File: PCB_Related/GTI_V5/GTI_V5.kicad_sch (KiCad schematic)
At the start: 165 parts, among them IC3 MAX253CSA+, IC4 AMC1306M25QDWVRQ1, IC5 AMC1306M25QDWVRQ1, IC6 AMC1306M25QDWVRQ1, IC7 MAX253CSA+, IC8 MAX253CSA+, IC9 AMC1306M25QDWVRQ1, J1 Screw_Terminal_01x03, J2 Screw_Terminal_01x02, J3 Screw_Terminal_01x02, J4 Conn_01x05_Male, J5 Conn_01x02_Male, J6 Conn_01x02_Male, K1 G5LE-1, K2 G5LE-1, Q1 BUZ11, Q2 2N7002, Q3 BUZ11, Q4 BUZ11, Q5 BUZ11, T1 760390014, T2 760390014, T3 760390014, U1 STM32L475RCTx, U2 UCC21520ADW, U3 AZ1117-5.0, U4 NCP1117-3.3_SOT223, U5 UCC21520ADW, Y1 Crystal_GND24

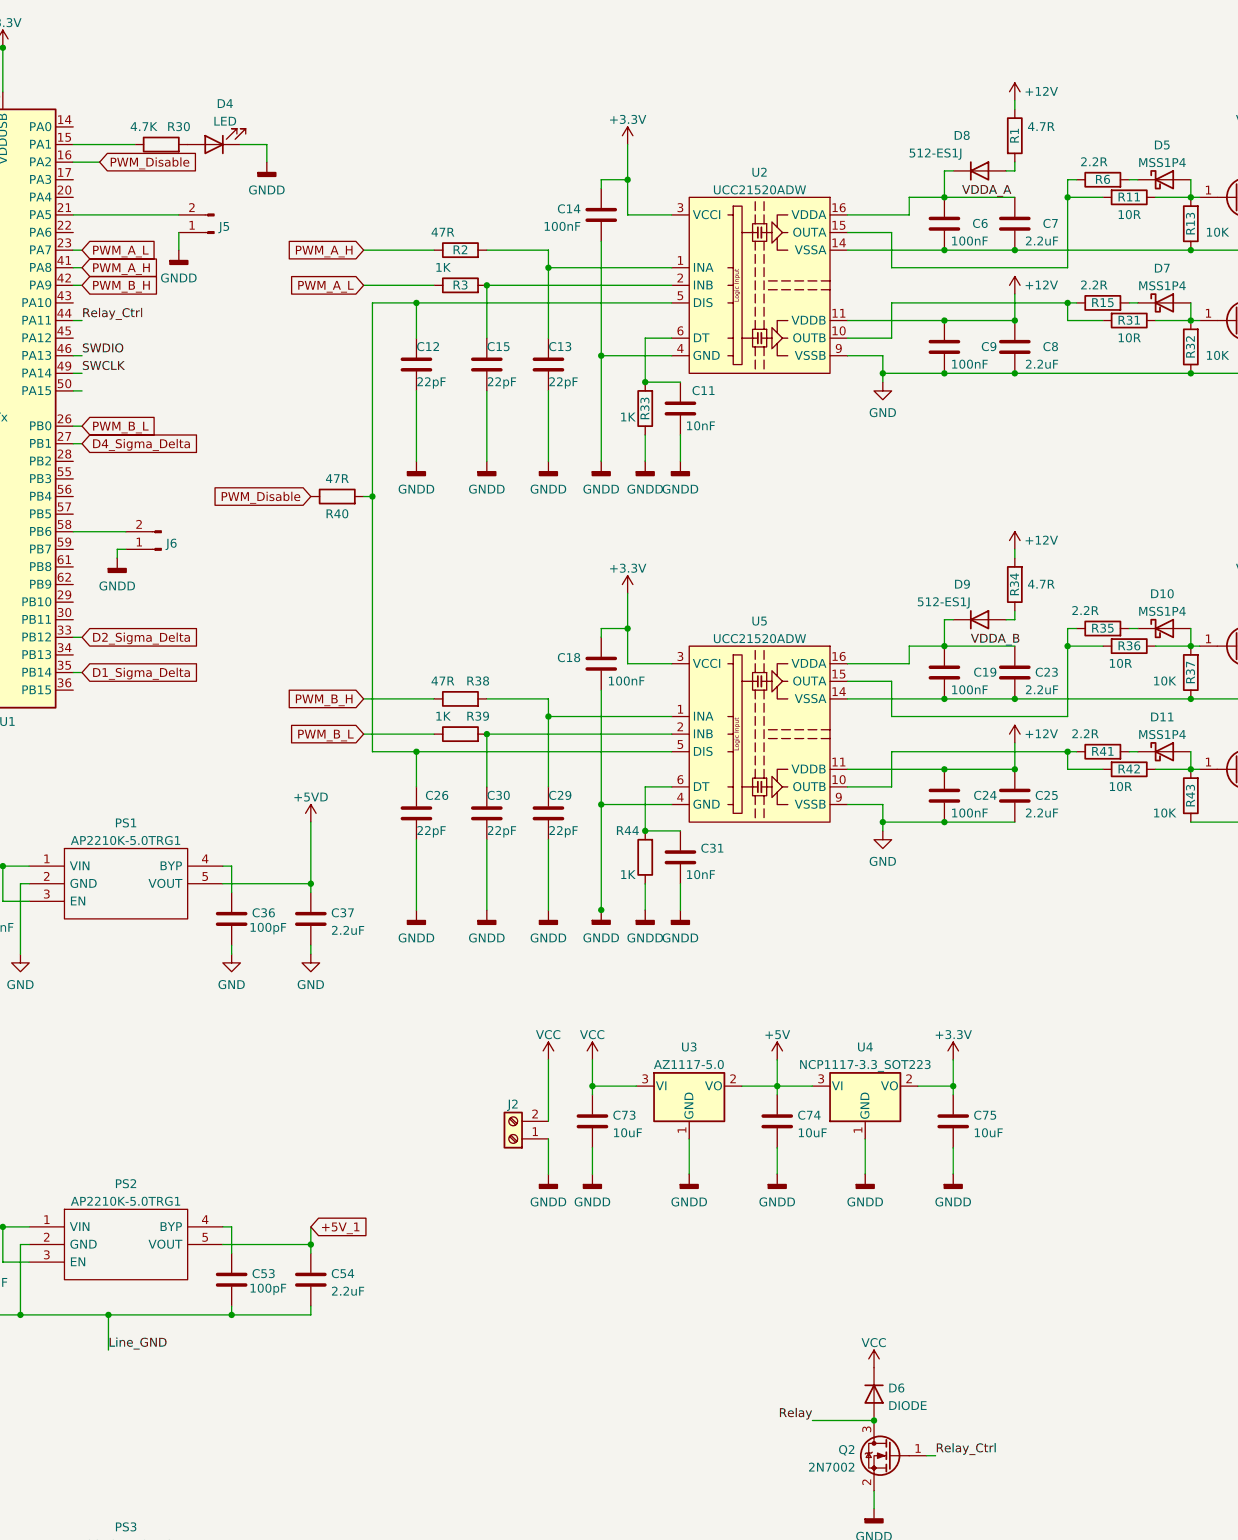
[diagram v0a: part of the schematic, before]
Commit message: PCB now assembled - with these component values
The hardware deadtime resistors on the UCC21520 are 4.7K for a 47ns deadtime. This can always be increased further in software on the STM32L475
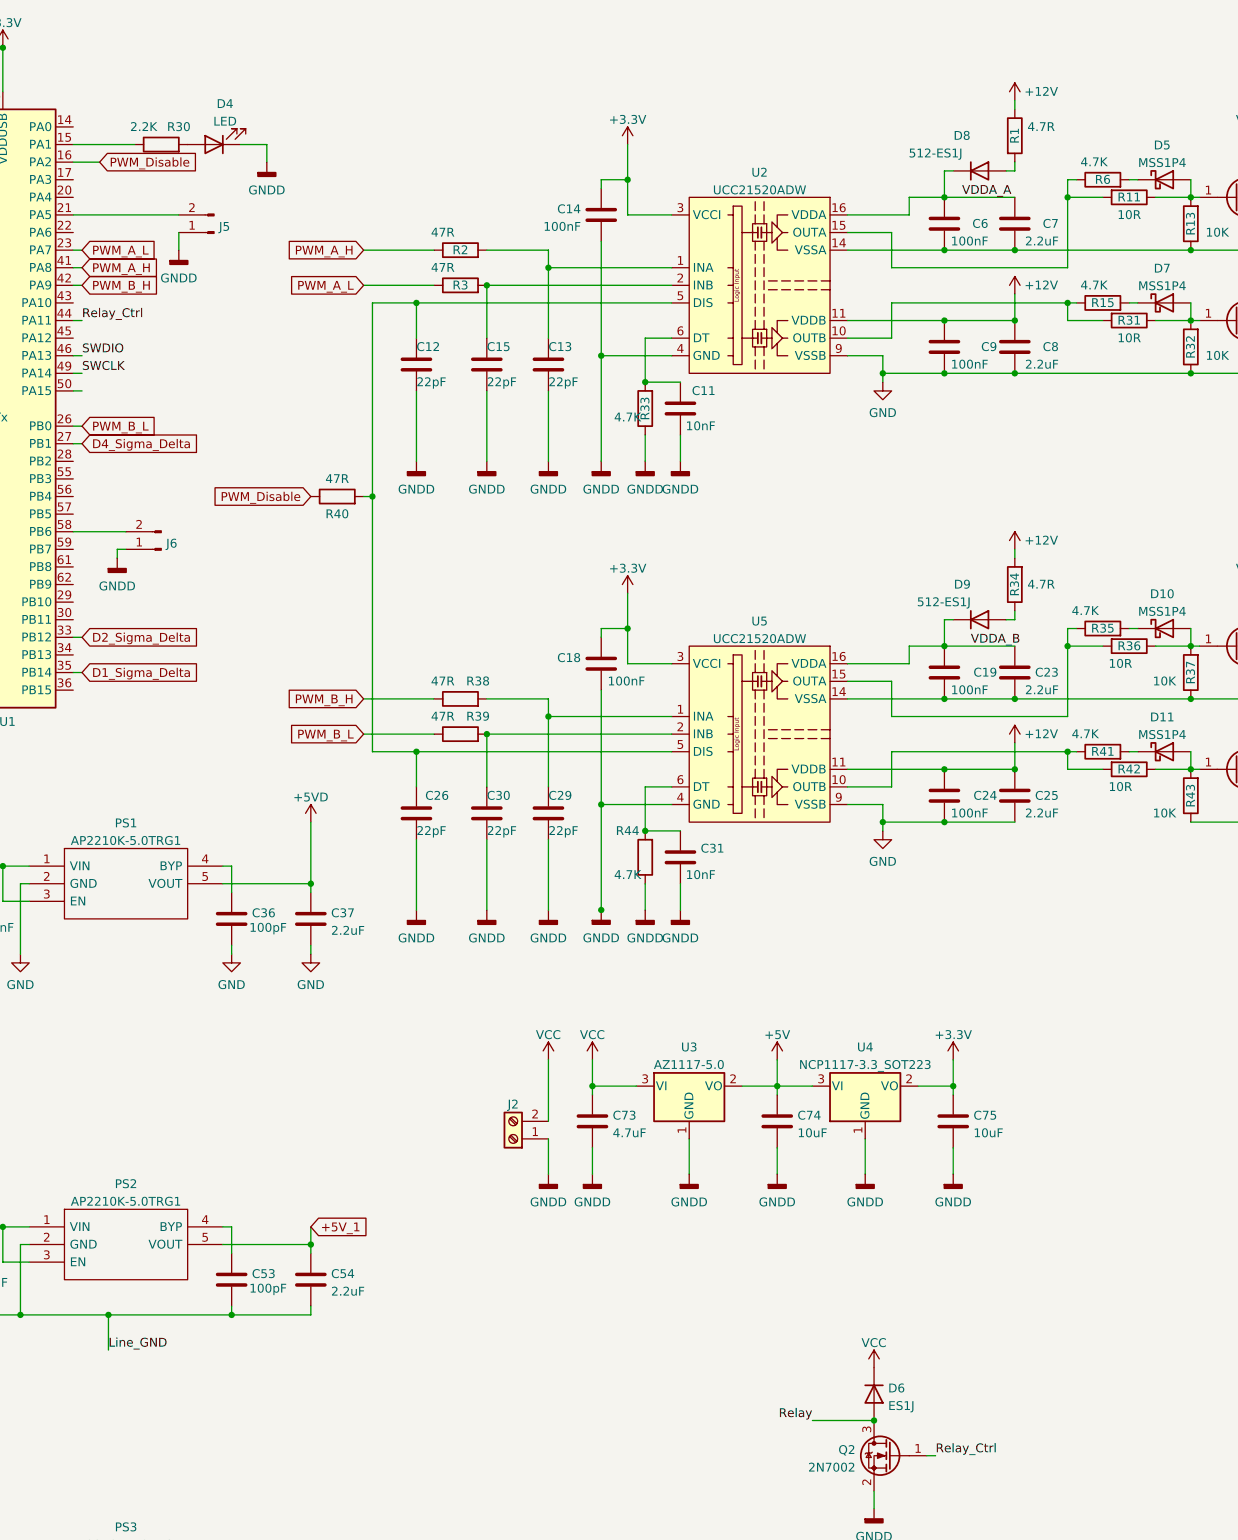
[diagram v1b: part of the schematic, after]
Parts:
- C73: value 10uF -> 4.7uF
- D6: value DIODE -> ES1J
- R15, R35, R41, R6: value 2.2R -> 4.7K
- R3, R39: value 1K -> 47R
- R30: value 4.7K -> 2.2K
- R33, R44: value 1K -> 4.7K
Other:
- company: (none) -> James Fotherby
- title: (none) -> GTI version 5
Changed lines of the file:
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@@
 (kicad_sch (version 20211123) (generator eeschema)
   (paper "A3")
+  (title_block
+    (title "GTI version 5")
+    (company "James Fotherby")
+  )
   (junction (at 88.9 20.32) (diameter 0) (color 0 0 0 0)
   )
@@
     (in_bom yes) (on_board yes)
     (property "Reference" "R30" (id 0) (at 116.84 31.75 90))
-    (property "Value" "4.7K" (id 1) (at 111.76 31.75 90))
+    (property "Value" "2.2K" (id 1) (at 111.76 31.75 90))
     (property "Footprint" "Resistor_SMD:R_0603_1608Metric" (id 2) (at 114.3 36.068 90)
       (effects (font (size 1.27 1.27)) hide)
@@
     (in_bom yes) (on_board yes)
     (property "Reference" "R15" (id 0) (at 250.19 57.15 90))
-    (property "Value" "2.2R" (id 1) (at 248.92 54.61 90))
+    (property "Value" "4.7K" (id 1) (at 248.92 54.61 90))
     (property "Footprint" "Resistor_SMD:R_0603_1608Metric" (id 2) (at 250.19 58.928 90)
       (effects (font (size 1.27 1.27)) hide)
@@
     (in_bom yes) (on_board yes)
     (property "Reference" "R35" (id 0) (at 250.19 104.14 90))
-    (property "Value" "2.2R" (id 1) (at 247.65 101.6 90))
+    (property "Value" "4.7K" (id 1) (at 247.65 101.6 90))
     (property "Footprint" "Resistor_SMD:R_0603_1608Metric" (id 2) (at 250.19 105.918 90)
       (effects (font (size 1.27 1.27)) hide)
@@
     (in_bom yes) (on_board yes)
     (property "Reference" "R39" (id 0) (at 160.02 116.84 90))
-    (property "Value" "1K" (id 1) (at 154.94 116.84 90))
+    (property "Value" "47R" (id 1) (at 154.94 116.84 90))
     (property "Footprint" "Resistor_SMD:R_0603_1608Metric" (id 2) (at 157.48 121.158 90)
       (effects (font (size 1.27 1.27)) hide)
@@
     (in_bom yes) (on_board yes)
     (property "Reference" "R6" (id 0) (at 250.19 39.37 90))
-    (property "Value" "2.2R" (id 1) (at 248.92 36.83 90))
+    (property "Value" "4.7K" (id 1) (at 248.92 36.83 90))
     (property "Footprint" "Resistor_SMD:R_0603_1608Metric" (id 2) (at 250.19 41.148 90)
       (effects (font (size 1.27 1.27)) hide)
@@
     (in_bom yes) (on_board yes)
     (property "Reference" "R33" (id 0) (at 184.15 72.39 90))
-    (property "Value" "1K" (id 1) (at 181.61 73.66 0))
+    (property "Value" "4.7K" (id 1) (at 181.61 73.66 0))
     (property "Footprint" "Resistor_SMD:R_0603_1608Metric" (id 2) (at 185.928 72.39 90)
       (effects (font (size 1.27 1.27)) hide)
@@
     (in_bom yes) (on_board yes)
     (property "Reference" "R3" (id 0) (at 157.48 54.61 90))
-    (property "Value" "1K" (id 1) (at 154.94 52.07 90))
+    (property "Value" "47R" (id 1) (at 154.94 52.07 90))
     (property "Footprint" "Resistor_SMD:R_0603_1608Metric" (id 2) (at 157.48 56.388 90)
       (effects (font (size 1.27 1.27)) hide)
@@
       (effects (font (size 1.27 1.27)) (justify left))
     )
-    (property "Value" "10uF" (id 1) (at 179.451 176.9622 0)
+    (property "Value" "4.7uF" (id 1) (at 179.451 176.9622 0)
       (effects (font (size 1.27 1.27)) (justify left))
     )
@@
     (in_bom yes) (on_board yes)
     (property "Reference" "R41" (id 0) (at 250.19 121.92 90))
-    (property "Value" "2.2R" (id 1) (at 247.65 119.38 90))
+    (property "Value" "4.7K" (id 1) (at 247.65 119.38 90))
     (property "Footprint" "Resistor_SMD:R_0603_1608Metric" (id 2) (at 250.19 123.698 90)
       (effects (font (size 1.27 1.27)) hide)
@@
       (effects (font (size 1.27 1.27)) (justify right))
     )
-    (property "Value" "DIODE" (id 1) (at 219.202 216.3322 90)
+    (property "Value" "ES1J" (id 1) (at 219.202 216.3322 90)
       (effects (font (size 1.27 1.27)) (justify right))
     )
@@
     (in_bom yes) (on_board yes)
     (property "Reference" "R44" (id 0) (at 181.61 133.35 0))
-    (property "Value" "1K" (id 1) (at 181.61 139.7 0))
+    (property "Value" "4.7K" (id 1) (at 181.61 139.7 0))
     (property "Footprint" "Resistor_SMD:R_0603_1608Metric" (id 2) (at 185.928 137.16 90)
       (effects (font (size 1.27 1.27)) hide)
@@
     )
     (path "/951b7b55-2863-405e-ae6d-1fd17c3ec689"
-      (reference "C73") (unit 1) (value "10uF") (footprint "Capacitor_SMD:C_0805_2012Metric")
+      (reference "C73") (unit 1) (value "4.7uF") (footprint "Capacitor_SMD:C_0805_2012Metric")
     )
     (path "/296111a0-ec60-4d3a-9cac-a894157b3ca8"
@@
     )
     (path "/d677406a-ac71-4fe4-a70c-dfe5c8f202ad"
-      (reference "D6") (unit 1) (value "DIODE") (footprint "ES1J:DIOM5227X250N")
+      (reference "D6") (unit 1) (value "ES1J") (footprint "ES1J:DIOM5227X250N")
     )
     (path "/fbba1de7-817e-40fe-9f64-fe1558764436"
@@
     )
     (path "/8c962d10-4f03-4433-aa53-f6139ceea479"
-      (reference "R3") (unit 1) (value "1K") (footprint "Resistor_SMD:R_0603_1608Metric")
+      (reference "R3") (unit 1) (value "47R") (footprint "Resistor_SMD:R_0603_1608Metric")
     )
     (path "/283fdcd3-581a-45f4-91d2-e5dac8b7a385"
@@
     )
     (path "/66c2e66c-020e-496c-b501-564e31c20967"
-      (reference "R6") (unit 1) (value "2.2R") (footprint "Resistor_SMD:R_0603_1608Metric")
+      (reference "R6") (unit 1) (value "4.7K") (footprint "Resistor_SMD:R_0603_1608Metric")
     )
     (path "/e4bf290b-a183-4fbe-880d-b39fd4cc4501"
@@
     )
     (path "/222cc94d-27b0-4109-8931-9de94cf867ed"
-      (reference "R15") (unit 1) (value "2.2R") (footprint "Resistor_SMD:R_0603_1608Metric")
+      (reference "R15") (unit 1) (value "4.7K") (footprint "Resistor_SMD:R_0603_1608Metric")
     )
     (path "/e7500aa4-f565-4598-89c2-283a3365f50c"
@@
     )
     (path "/2140488f-7157-4d9b-9501-08c6ef652621"
-      (reference "R30") (unit 1) (value "4.7K") (footprint "Resistor_SMD:R_0603_1608Metric")
+      (reference "R30") (unit 1) (value "2.2K") (footprint "Resistor_SMD:R_0603_1608Metric")
     )
     (path "/62189345-7502-4b51-a955-4f200f34ba12"
@@
     )
     (path "/7a8dadd9-f549-41f1-b8d1-37726e763a49"
-      (reference "R33") (unit 1) (value "1K") (footprint "Resistor_SMD:R_0603_1608Metric")
+      (reference "R33") (unit 1) (value "4.7K") (footprint "Resistor_SMD:R_0603_1608Metric")
     )
     (path "/092bd28a-93db-4058-ba4e-4aa8f507e8b8"
@@
     )
     (path "/2e6f0acf-79b1-4916-bfd7-0f21207f4b33"
-      (reference "R35") (unit 1) (value "2.2R") (footprint "Resistor_SMD:R_0603_1608Metric")
+      (reference "R35") (unit 1) (value "4.7K") (footprint "Resistor_SMD:R_0603_1608Metric")
     )
     (path "/c3371546-d6e7-487b-b204-99d484d7be61"
@@
     )
     (path "/439ae41a-ba14-4839-a9ed-b0a2329decf0"
-      (reference "R39") (unit 1) (value "1K") (footprint "Resistor_SMD:R_0603_1608Metric")
+      (reference "R39") (unit 1) (value "47R") (footprint "Resistor_SMD:R_0603_1608Metric")
     )
     (path "/b01f53bc-9ba4-48eb-a190-0df49d6d0c72"
@@
     )
     (path "/a001724e-3f47-4935-8b09-172210c3b4f6"
-      (reference "R41") (unit 1) (value "2.2R") (footprint "Resistor_SMD:R_0603_1608Metric")
+      (reference "R41") (unit 1) (value "4.7K") (footprint "Resistor_SMD:R_0603_1608Metric")
     )
     (path "/d6b886c7-9013-4f82-8a77-0f789fc83d77"
@@
     )
     (path "/fd7210f0-501a-4e07-92f4-098546800f36"
-      (reference "R44") (unit 1) (value "1K") (footprint "Resistor_SMD:R_0603_1608Metric")
+      (reference "R44") (unit 1) (value "4.7K") (footprint "Resistor_SMD:R_0603_1608Metric")
     )
     (path "/1eacc8a9-30b0-4288-be32-2c09187912e8"
